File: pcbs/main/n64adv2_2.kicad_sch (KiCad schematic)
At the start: 70 parts, among them U10 TLV70225DBV, U11 TLV70025DDC

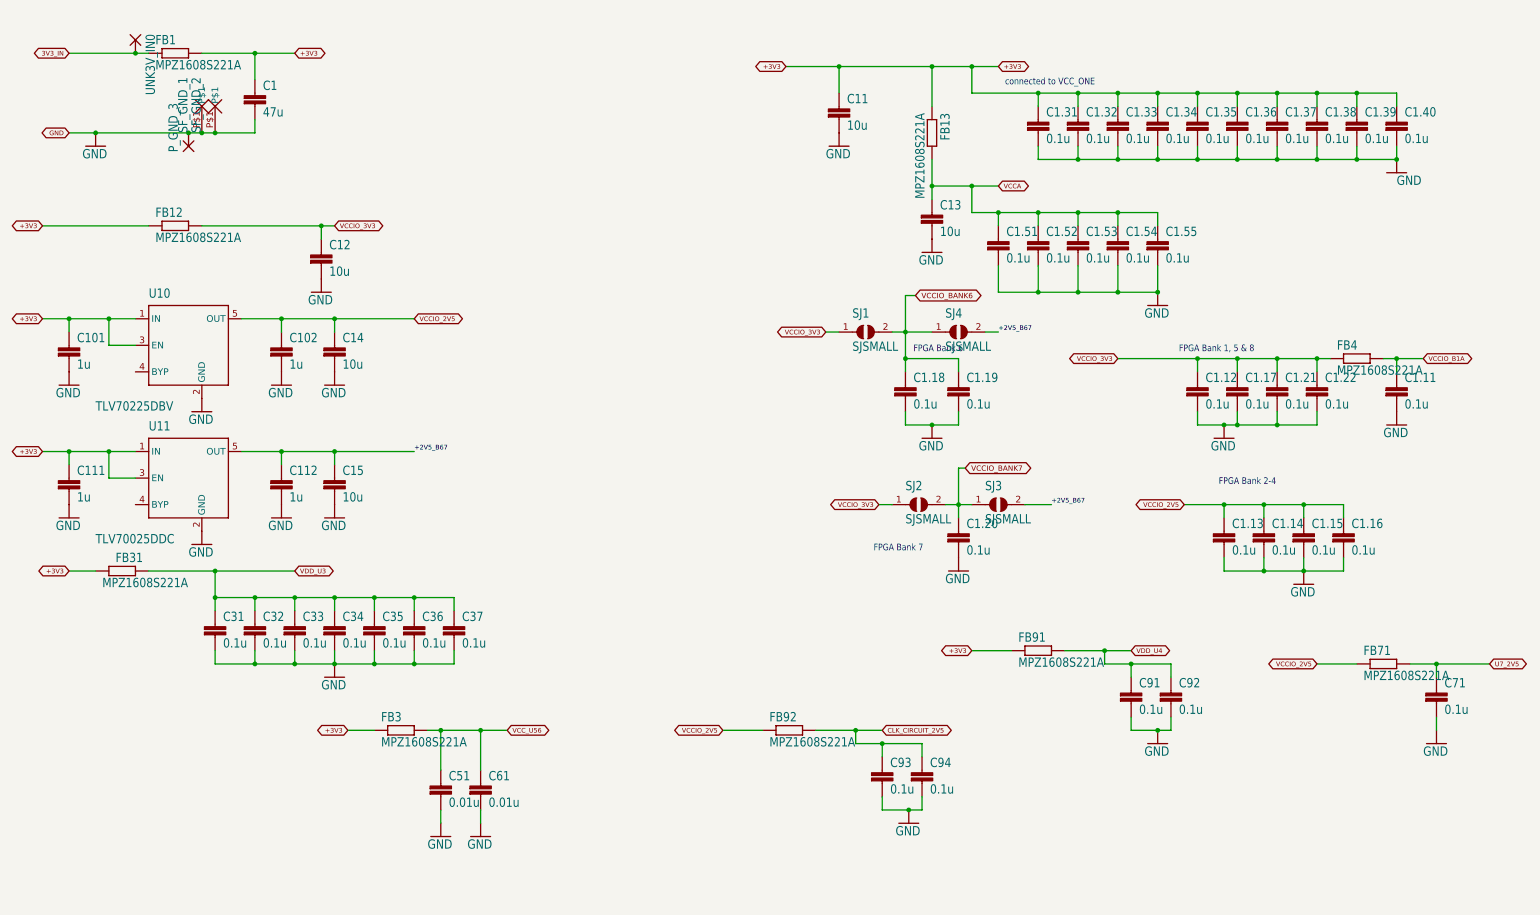
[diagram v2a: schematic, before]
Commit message: update main-pcb: - remove jumper which were left overs from prototype stages - remove some test points - add pads for SPDIF near DIY-IO-Pad area
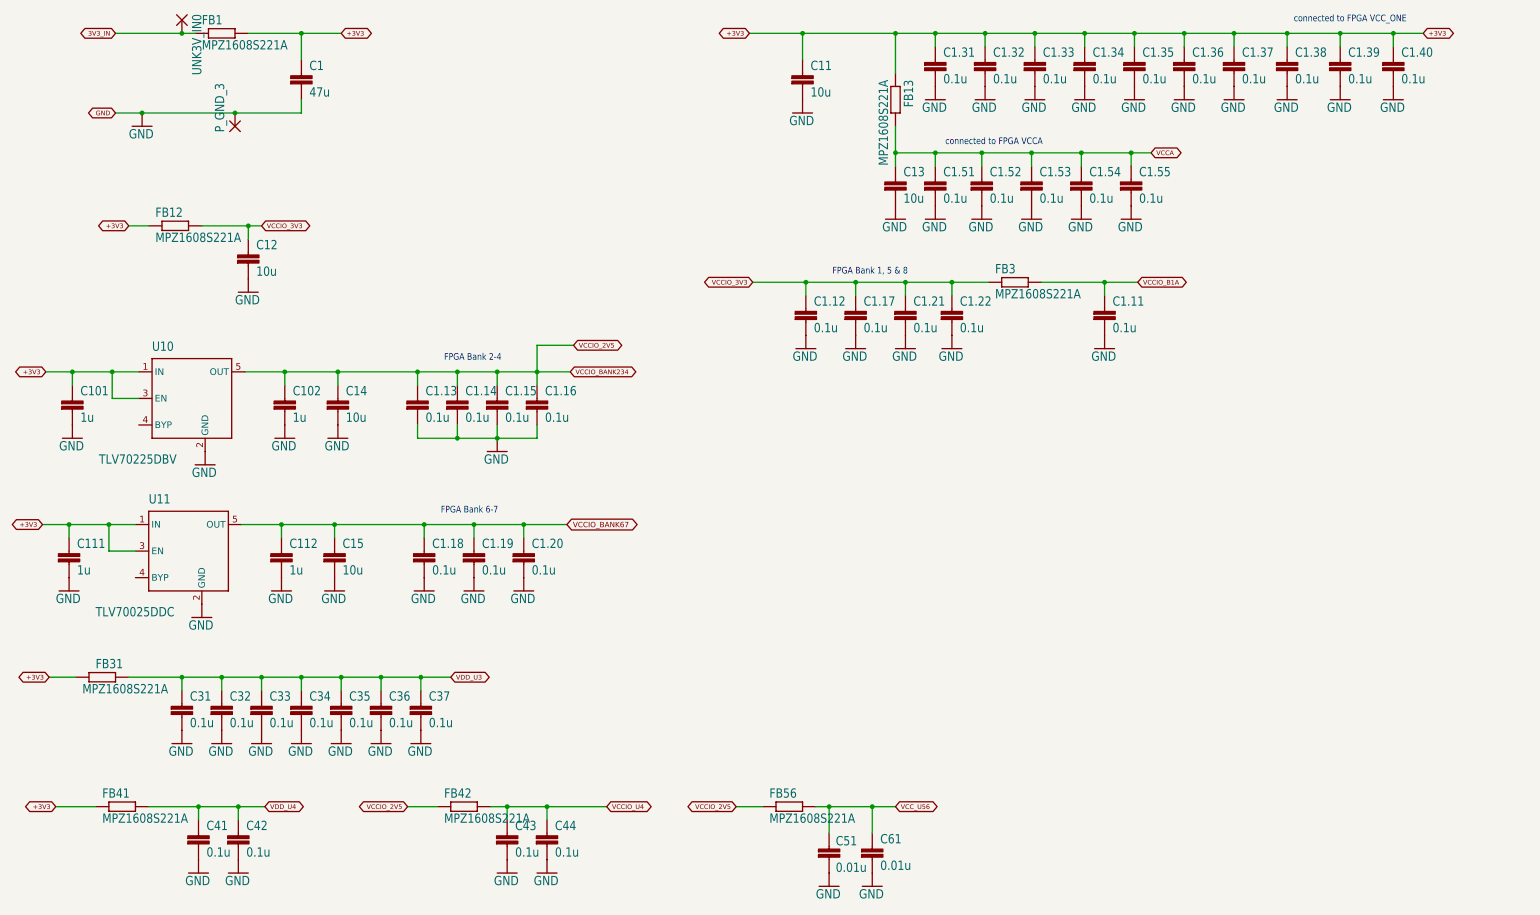
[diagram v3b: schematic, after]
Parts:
- removed C71: 0.1u, n64adv2:C0603, symbol n64adv2-eagle-import:C-EUC0603
- removed FB71: MPZ1608S221A, n64adv2:R0603, symbol n64adv2-eagle-import:R-EU_R0603
- removed SF_GND_1, SF_GND_2: PADSHIELD_FINGER, n64adv2:GND_FINGER_PAD, symbol n64adv2-eagle-import:PADSHIELD_FINGER
- removed SJ1, SJ2, SJ3, SJ4: SJSMALL, n64adv2:SJ_SMALL, symbol n64adv2-eagle-import:SJSMALL
- renumbered C91 to C41, C92 to C42, C93 to C43, C94 to C44, FB4 to FB3, FB91 to FB41, FB92 to FB42, FB3 to FB56
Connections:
- net VCCIO_BANK6 is gone; now on net VCCIO_BANK67: C1.18.1, C1.19.1
- net VCCIO_BANK7 is gone; now on net VCCIO_BANK67: C1.20.1
- net +3V3: no longer FB56.1
- net VCCIO_2V5: now also FB56.1
- net +2V5_B67 renamed VCCIO_BANK67
- net CLK_CIRCUIT_2V5 renamed VCCIO_U4
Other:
- note added: "FPGA Bank 6-7"
- note added: "connected to FPGA VCCA"
- note added: "connected to FPGA VCC_ONE"
- note removed: "FPGA Bank 6"
- note removed: "FPGA Bank 7"
- note removed: "connected to VCC_ONE"
- title: N64Adv2 (ADV7513) -> N64Adv2
- moved on the sheet: C1, C1.11, C1.12, C1.13, C1.14, C1.15, C1.16, C1.17, C1.18, C1.19, C1.20, C1.21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

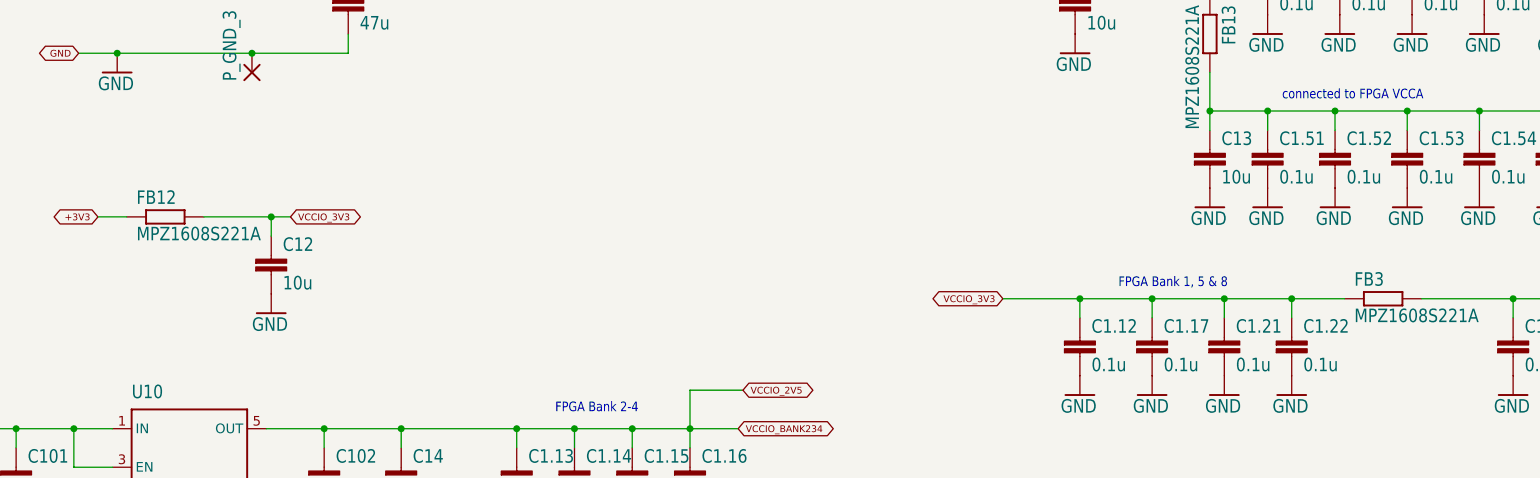
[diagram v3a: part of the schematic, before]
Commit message: Update main-PCB: - fixing solder mask - slightly move components a bit (USB port, JTAG, C2, ...)
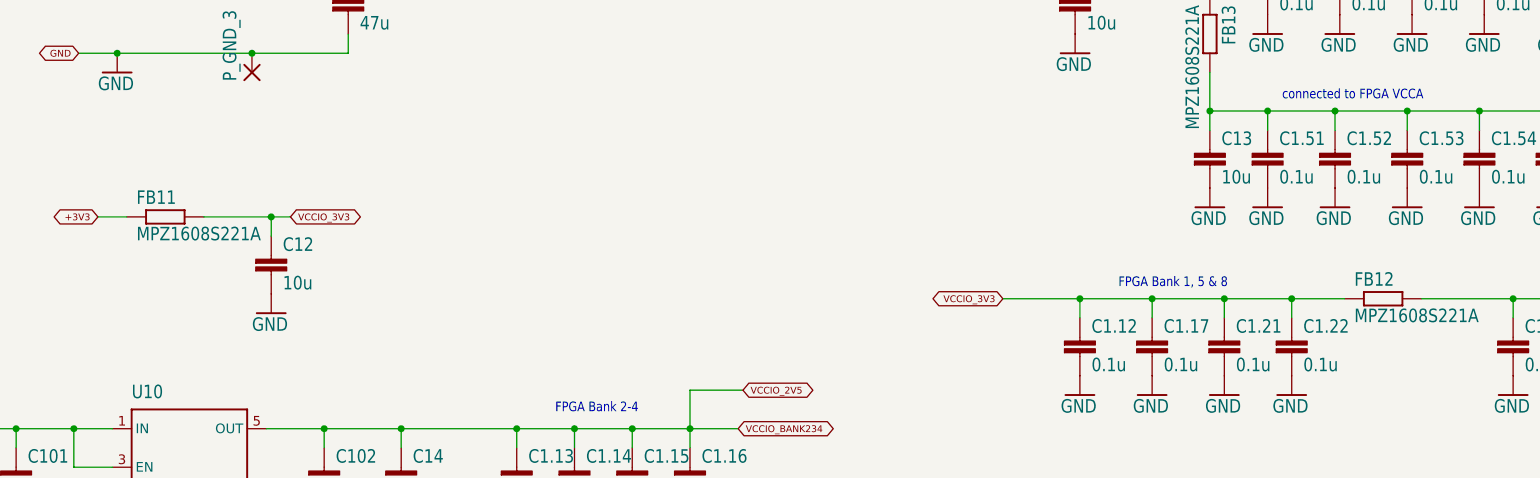
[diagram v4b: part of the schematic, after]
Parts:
- renumbered FB12 to FB11, FB3 to FB12
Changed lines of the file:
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@@
   (symbol (lib_id "n64adv2-eagle-import:R-EU_R0603") (at 208.915 74.295 0) (unit 1)
     (in_bom yes) (on_board yes)
-    (property "Reference" "FB3" (id 0) (at 205.105 72.7964 0)
+    (property "Reference" "FB12" (id 0) (at 205.105 72.7964 0)
       (effects (font (size 1.778 1.5113)) (justify left bottom))
     )
@@
   (symbol (lib_id "n64adv2-eagle-import:R-EU_R0603") (at 48.26 63.5 0) (unit 1)
     (in_bom yes) (on_board yes)
-    (property "Reference" "FB12" (id 0) (at 44.45 62.0014 0)
-      (effects (font (size 1.778 1.5113)) (justify left bottom))
-    )
+    (property "Reference" "FB11" (id 0) (at 44.45 62.0014 0)
+      (effects (font (size 1.778 1.5113)) (justify left bottom))
+    )
